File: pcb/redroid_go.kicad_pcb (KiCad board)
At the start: 2 copper layers, 70 x 95 mm, 100 parts, among them J1 USB4105-GF-A, J2 5051101892, J3 Conn_01x02_Pin, J4 Conn_01x10_Pin, Q1 UMH3N, Q2 PMOS, Q3 UMH3N, SW1 UP, SW10 A, SW11 SW_SPDT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

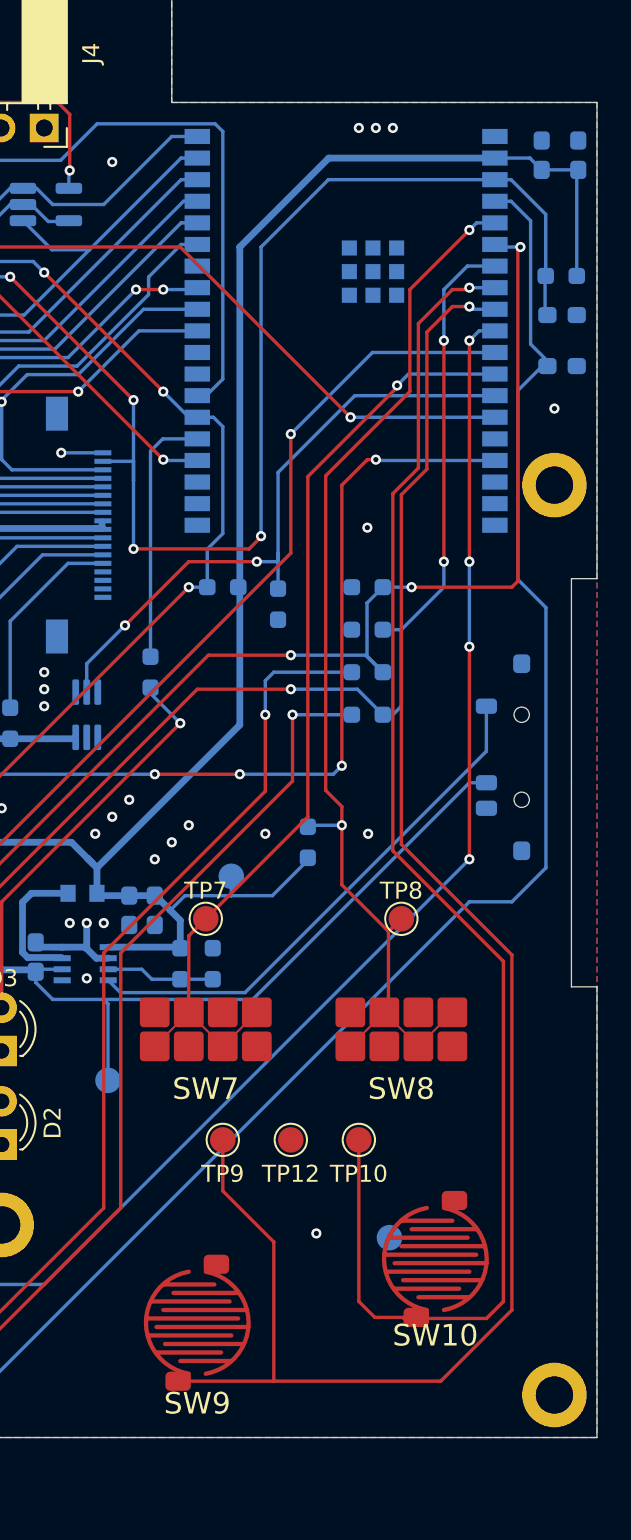
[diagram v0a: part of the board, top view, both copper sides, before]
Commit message: Other fix in switch position
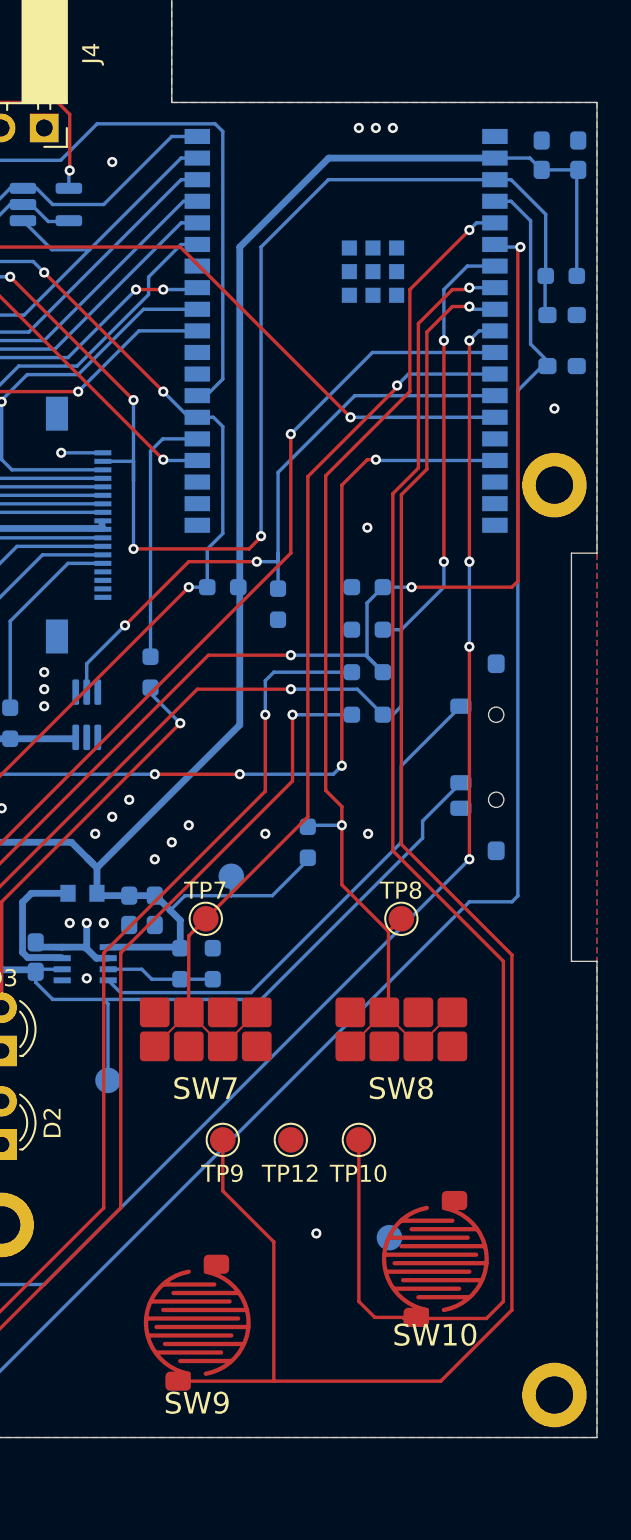
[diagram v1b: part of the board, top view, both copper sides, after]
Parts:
- moved SW11 1.50 mm to (198.0, 85.5)
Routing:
- net IO36: track 97.9 -> 96.6 mm
- net Net-(SW11-B): track 41.7 -> 40.7 mm
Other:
- outline, holes or cut-outs redrawn
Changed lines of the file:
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@@
 	(footprint "MK-12F03-G015:MK-12F03-G015"
 		(layer "B.Cu")
-		(at 199.5 85.5 -90)
+		(at 198 85.5 -90)
 		(property "Reference" "SW11"
 			(at 2.5 9 90)
@@
 	)
 	(gr_line
-		(start 197 78)
-		(end 198.5 78)
+		(start 197 76.5)
+		(end 198.5 76.5)
 		(stroke
 			(width 0.05)
@@
 	)
 	(gr_line
-		(start 197 90)
-		(end 197 102)
+		(start 197 88.5)
+		(end 197 100.5)
 		(stroke
 			(width 0.05)
@@
 	)
 	(gr_line
-		(start 197 102)
-		(end 198.5 102)
+		(start 197 100.5)
+		(end 198.5 100.5)
 		(stroke
 			(width 0.05)
@@
 	)
 	(gr_line
-		(start 197 90)
-		(end 197 78)
+		(start 197 88.5)
+		(end 197 76.5)
 		(stroke
 			(width 0.05)
-			(type default)
+			(type solid)
 		)
 		(layer "Edge.Cuts")
@@
 	(gr_line
 		(start 198.5 50)
-		(end 198.5 78)
+		(end 198.5 76.5)
 		(stroke
 			(width 0.05)
@@
 	)
 	(gr_line
-		(start 198.5 102)
+		(start 198.5 100.5)
 		(end 198.5 128.5)
 		(stroke
@@
 	)
 	(segment
-		(start 178.259551 102.740449)
-		(end 191 90)
+		(start 178.759551 102.740449)
+		(end 188.25 93.25)
 		(width 0.2)
 		(layer "B.Cu")
@@
 	)
 	(segment
-		(start 191 90)
-		(end 192 90)
+		(start 165.5 101.740449)
+		(end 165.5 101.1125)
 		(width 0.2)
 		(layer "B.Cu")
@@
 	)
 	(segment
-		(start 165.5 101.740449)
-		(end 165.5 101.1125)
+		(start 167.057201 100.96545)
+		(end 165.64705 100.96545)
 		(width 0.2)
 		(layer "B.Cu")
@@
 	)
 	(segment
-		(start 167.057201 100.96545)
-		(end 165.64705 100.96545)
+		(start 188.25 93.25)
+		(end 188.25 92.25)
 		(width 0.2)
 		(layer "B.Cu")
@@
 	)
 	(segment
-		(start 163.0375 101)
-		(end 165 101)
-		(width 0.4)
+		(start 188.25 92.25)
+		(end 190.5 90)
+		(width 0.2)
 		(layer "B.Cu")
 		(net 4)
 	)
 	(segment
-		(start 169.5 102.740449)
-		(end 178.259551 102.740449)
-		(width 0.2)
+		(start 163.0375 101)
+		(end 165 101)
+		(width 0.4)
 		(layer "B.Cu")
 		(net 4)
@@
 	)
 	(segment
+		(start 169.5 102.740449)
+		(end 178.759551 102.740449)
+		(width 0.2)
+		(layer "B.Cu")
+		(net 4)
+	)
+	(segment
 		(start 136.5 52)
 		(end 137 51.5)
@@
 	)
 	(segment
-		(start 156.4125 127.5875)
-		(end 156.4125 128)
-		(width 0.2)
-		(layer "B.Cu")
-		(net 13)
-	)
-	(segment
-		(start 195.5 95)
-		(end 193.5 97)
-		(width 0.2)
-		(layer "B.Cu")
-		(net 13)
-	)
-	(segment
 		(start 156.4125 128)
 		(end 156.4125 130.5)
@@
 	)
 	(segment
-		(start 193.4493 55.81)
-		(end 194.6 56.9607)
+		(start 191 97)
+		(end 161.5 126.5)
 		(width 0.2)
 		(layer "B.Cu")
@@
 	)
 	(segment
-		(start 157.5 126.5)
-		(end 156.4125 127.5875)
+		(start 194.6 64.2125)
+		(end 195.5875 65.2)
 		(width 0.2)
 		(layer "B.Cu")
@@
 	)
 	(segment
-		(start 191 97)
-		(end 161.5 126.5)
+		(start 195.5875 65.2)
+		(end 193.85 66.9375)
 		(width 0.2)
 		(layer "B.Cu")
@@
 	)
 	(segment
-		(start 193.5 97)
-		(end 191 97)
+		(start 194.6 56.9607)
+		(end 194.6 64.2125)
 		(width 0.2)
 		(layer "B.Cu")
@@
 	)
 	(segment
-		(start 193.85 66.9375)
-		(end 193.85 78.051304)
+		(start 161.5 126.5)
+		(end 157.5 126.5)
 		(width 0.2)
 		(layer "B.Cu")
@@
 	)
 	(segment
-		(start 195.5875 65.2)
-		(end 193.85 66.9375)
+		(start 193.85 96.65)
+		(end 193.5 97)
 		(width 0.2)
 		(layer "B.Cu")
@@
 	)
 	(segment
-		(start 161.5 126.5)
-		(end 157.5 126.5)
+		(start 192.5 55.81)
+		(end 193.4493 55.81)
 		(width 0.2)
 		(layer "B.Cu")
@@
 	)
 	(segment
-		(start 192.5 55.81)
-		(end 193.4493 55.81)
+		(start 193.4493 55.81)
+		(end 194.6 56.9607)
 		(width 0.2)
 		(layer "B.Cu")
@@
 	)
 	(segment
-		(start 194.6 64.2125)
-		(end 195.5875 65.2)
+		(start 193.85 66.9375)
+		(end 193.85 96.65)
 		(width 0.2)
 		(layer "B.Cu")
@@
 	)
 	(segment
-		(start 193.85 78.051304)
-		(end 195.5 79.701304)
+		(start 157.5 126.5)
+		(end 156.4125 127.5875)
 		(width 0.2)
 		(layer "B.Cu")
@@
 	)
 	(segment
-		(start 195.5 79.701304)
-		(end 195.5 95)
+		(start 156.4125 127.5875)
+		(end 156.4125 128)
 		(width 0.2)
 		(layer "B.Cu")
@@
 	)
 	(segment
-		(start 194.6 56.9607)
-		(end 194.6 64.2125)
+		(start 193.5 97)
+		(end 191 97)
 		(width 0.2)
 		(layer "B.Cu")
@@
 	)
 	(segment
-		(start 169.763697 101.615448)
-		(end 170.488698 102.340449)
+		(start 170.488698 102.340449)
+		(end 178.159551 102.340449)
 		(width 0.2)
 		(layer "B.Cu")
@@
 	)
 	(segment
-		(start 170.488698 102.340449)
-		(end 177.807881 102.340449)
+		(start 178.159551 102.340449)
+		(end 187 93.5)
 		(width 0.2)
 		(layer "B.Cu")
@@
 	)
 	(segment
-		(start 177.807881 102.340449)
-		(end 192 88.14833)
+		(start 187 89)
+		(end 190.5 85.5)
 		(width 0.2)
 		(layer "B.Cu")
@@
 	)
 	(segment
-		(start 192 88.14833)
-		(end 192 85.5)
+		(start 187 93.5)
+		(end 187 89)
+		(width 0.2)
+		(layer "B.Cu")
+		(net 66)
+	)
+	(segment
+		(start 169.763697 101.615448)
+		(end 170.488698 102.340449)
 		(width 0.2)
 		(layer "B.Cu")

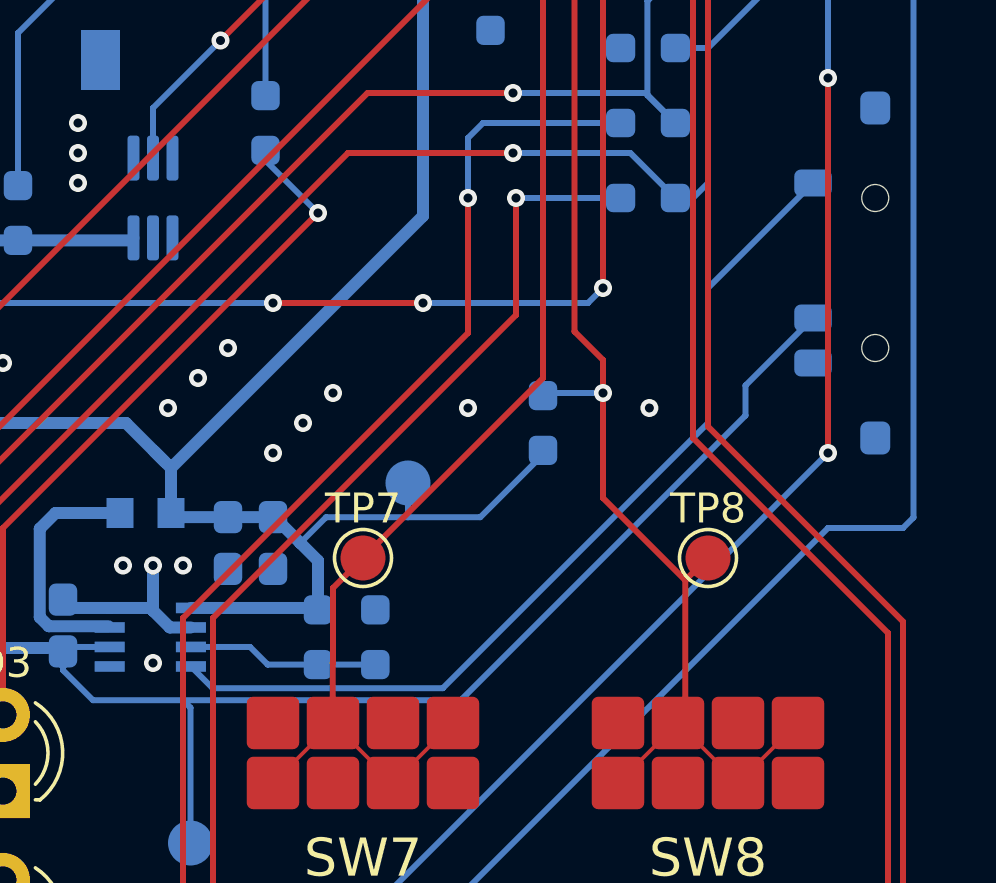
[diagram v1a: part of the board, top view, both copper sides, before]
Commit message: Change switch connection to improve PCB
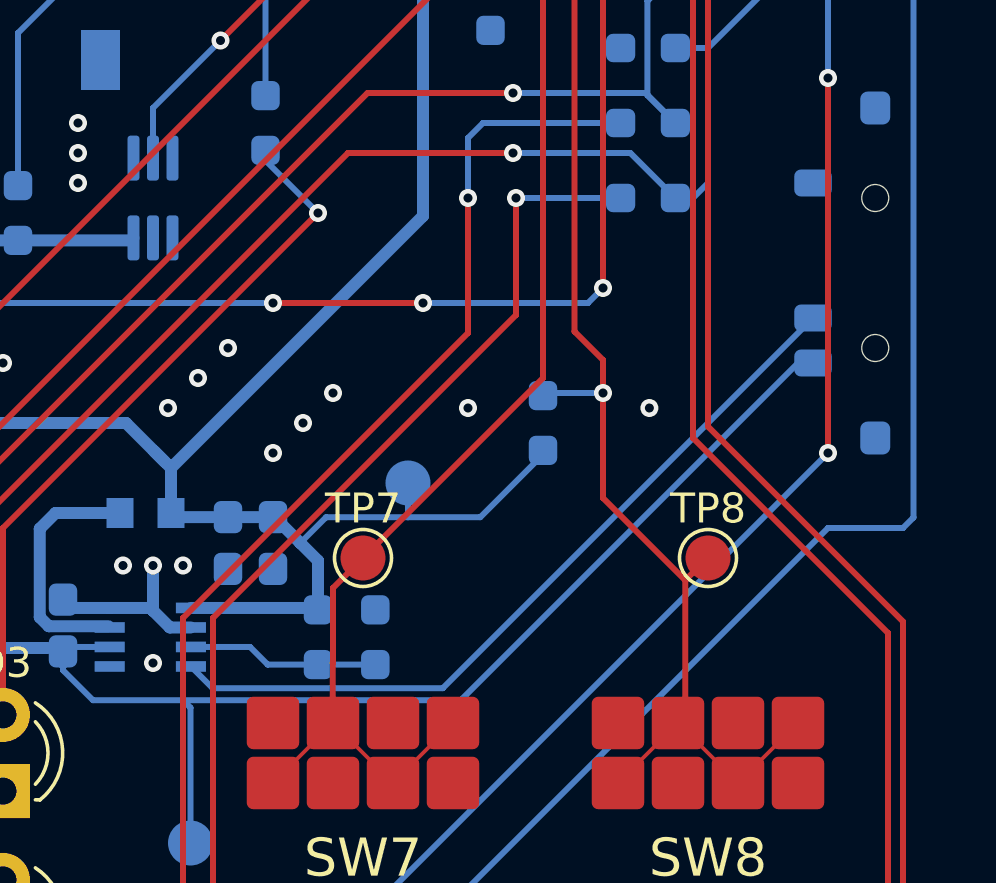
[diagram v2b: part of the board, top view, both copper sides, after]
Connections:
- C2 pad 1: Net-(SW11-B) -> Net-(SW11-C)
- F1 pad 2: Net-(SW11-B) -> Net-(SW11-C)
- SW11 pad 1: Net-(SW11-A) -> unconnected-(SW11-A-Pad1)
- SW11 pad 3: unconnected-(SW11-C-Pad3) -> Net-(SW11-C)
- TP2 pad 1: Net-(SW11-B) -> Net-(SW11-C)
- U3 pad 2: Net-(SW11-B) -> Net-(SW11-C)
- U3 pad 8: Net-(SW11-A) -> Net-(SW11-B)
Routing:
- net Net-(SW11-C): track 0.00 -> 39.5 mm
- net Net-(SW11-A): track 30.6 -> 0.00 mm
- net Net-(SW11-B): track 40.7 -> 26.1 mm
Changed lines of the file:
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@@
 	(net 63 "IO33")
 	(net 64 "IO32")
-	(net 65 "unconnected-(SW11-C-Pad3)")
-	(net 66 "Net-(SW11-A)")
+	(net 65 "unconnected-(SW11-A-Pad1)")
+	(net 66 "Net-(SW11-C)")
 	(net 67 "unconnected-(U1-NC-Pad19)")
 	(net 68 "unconnected-(U1-NC-Pad27)")
@@
 			(size 1.004699 0.3556)
 			(layers "B.Cu" "B.Mask" "B.Paste")
-			(net 4 "Net-(SW11-B)")
+			(net 66 "Net-(SW11-C)")
 			(pinfunction "VIN")
 			(pintype "unspecified")
@@
 			(size 1.004699 0.3556)
 			(layers "B.Cu" "B.Mask" "B.Paste")
-			(net 66 "Net-(SW11-A)")
+			(net 4 "Net-(SW11-B)")
 			(pinfunction "EN")
 			(pintype "unspecified")
@@
 			(layers "B.Cu" "B.Mask" "B.Paste")
 			(roundrect_rratio 0.25)
-			(net 66 "Net-(SW11-A)")
+			(net 65 "unconnected-(SW11-A-Pad1)")
 			(pinfunction "A")
 			(pintype "passive")
@@
 			(layers "B.Cu" "B.Mask" "B.Paste")
 			(roundrect_rratio 0.25)
-			(net 65 "unconnected-(SW11-C-Pad3)")
+			(net 66 "Net-(SW11-C)")
 			(pinfunction "C")
 			(pintype "passive")
@@
 			(layers "B.Cu" "B.Mask" "B.Paste")
 			(roundrect_rratio 0.25)
-			(net 4 "Net-(SW11-B)")
+			(net 66 "Net-(SW11-C)")
 			(pintype "passive")
 		)
@@
 			(size 1.5 1.5)
 			(layers "B.Cu" "B.Mask")
-			(net 4 "Net-(SW11-B)")
+			(net 66 "Net-(SW11-C)")
 			(pinfunction "1")
 			(pintype "passive")
@@
 			(layers "B.Cu" "B.Mask" "B.Paste")
 			(roundrect_rratio 0.25)
-			(net 4 "Net-(SW11-B)")
+			(net 66 "Net-(SW11-C)")
 			(pintype "passive")
 		)
@@
 	)
 	(segment
-		(start 178.759551 102.740449)
-		(end 188.25 93.25)
-		(width 0.2)
-		(layer "B.Cu")
-		(net 4)
-	)
-	(segment
-		(start 166.5 102.740449)
-		(end 165.5 101.740449)
-		(width 0.2)
-		(layer "B.Cu")
-		(net 4)
-	)
-	(segment
-		(start 165.5 101.740449)
-		(end 165.5 101.1125)
-		(width 0.2)
-		(layer "B.Cu")
-		(net 4)
-	)
-	(segment
-		(start 167.057201 100.96545)
-		(end 165.64705 100.96545)
-		(width 0.2)
-		(layer "B.Cu")
-		(net 4)
-	)
-	(segment
-		(start 188.25 93.25)
-		(end 188.25 92.25)
-		(width 0.2)
-		(layer "B.Cu")
-		(net 4)
-	)
-	(segment
-		(start 165.64705 100.96545)
-		(end 165.5 101.1125)
-		(width 0.2)
-		(layer "B.Cu")
-		(net 4)
-	)
-	(segment
-		(start 169.75 107.5)
-		(end 169.75 102.990449)
-		(width 0.2)
-		(layer "B.Cu")
-		(net 4)
-	)
-	(segment
-		(start 188.25 92.25)
-		(end 190.5 90)
-		(width 0.2)
-		(layer "B.Cu")
-		(net 4)
-	)
-	(segment
-		(start 163.0375 101)
-		(end 165 101)
-		(width 0.4)
-		(layer "B.Cu")
-		(net 4)
-	)
-	(segment
-		(start 169.75 102.990449)
-		(end 169.5 102.740449)
+		(start 170.488698 102.340449)
+		(end 169.763697 101.615448)
 		(width 0.2)
 		(layer "B.Cu")
@@
 	)
 	(segment
-		(start 166.5 102.740449)
-		(end 169.5 102.740449)
+		(start 178.159551 102.340449)
+		(end 170.488698 102.340449)
 		(width 0.2)
 		(layer "B.Cu")
@@
 	)
 	(segment
-		(start 165.5 101.5)
-		(end 165.5 101.1125)
-		(width 0.4)
-		(layer "B.Cu")
-		(net 4)
-	)
-	(segment
-		(start 169.5 102.740449)
-		(end 178.759551 102.740449)
+		(start 190.5 90)
+		(end 178.159551 102.340449)
 		(width 0.2)
 		(layer "B.Cu")
@@
 	)
 	(segment
-		(start 170.488698 102.340449)
-		(end 178.159551 102.340449)
+		(start 190 91.5)
+		(end 178.759551 102.740449)
 		(width 0.2)
 		(layer "B.Cu")
@@
 	)
 	(segment
-		(start 178.159551 102.340449)
-		(end 187 93.5)
+		(start 166.5 102.740449)
+		(end 165.5 101.740449)
 		(width 0.2)
 		(layer "B.Cu")
@@
 	)
 	(segment
-		(start 187 89)
-		(end 190.5 85.5)
+		(start 178.759551 102.740449)
+		(end 169.5 102.740449)
 		(width 0.2)
 		(layer "B.Cu")
@@
 	)
 	(segment
-		(start 187 93.5)
-		(end 187 89)
+		(start 165.5 101.740449)
+		(end 165.5 101.1125)
 		(width 0.2)
 		(layer "B.Cu")
@@
 	)
 	(segment
-		(start 169.763697 101.615448)
-		(end 170.488698 102.340449)
+		(start 167.057201 100.96545)
+		(end 165.64705 100.96545)
 		(width 0.2)
 		(layer "B.Cu")
 		(net 66)
+	)
+	(segment
+		(start 165.64705 100.96545)
+		(end 165.5 101.1125)
+		(width 0.2)
+		(layer "B.Cu")
+		(net 66)
+	)
+	(segment
+		(start 169.75 107.5)
+		(end 169.75 102.990449)
+		(width 0.2)
+		(layer "B.Cu")
+		(net 66)
+	)
+	(segment
+		(start 163.0375 101)
+		(end 165 101)
+		(width 0.4)
+		(layer "B.Cu")
+		(net 66)
+	)
+	(segment
+		(start 190.5 91.5)
+		(end 190 91.5)
+		(width 0.2)
+		(layer "B.Cu")
+		(net 66)
+	)
+	(segment
+		(start 169.75 102.990449)
+		(end 169.5 102.740449)
+		(width 0.2)
+		(layer "B.Cu")
+		(net 66)
+	)
+	(segment
+		(start 166.5 102.740449)
+		(end 169.5 102.740449)
+		(width 0.2)
+		(layer "B.Cu")
+		(net 66)
+	)
+	(segment
+		(start 165.5 101.5)
+		(end 165.5 101.1125)
+		(width 0.4)
+		(layer "B.Cu")
+		(net 66)
